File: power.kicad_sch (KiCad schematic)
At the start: 43 parts, among them SW2 SW_DPST

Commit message: more traces
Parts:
- added C49: 220uF, Capacitor_THT:CP_Radial_Tantal_D8.0mm_P5.00mm, symbol Device:C_Polarized_Small
- added C70: 33nF, Capacitor_SMD:C_0805_2012Metric, symbol Device:C_Small
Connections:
- net +5C: now also C70.2
- net +5V: now also C49.1
- net GND: now also C49.2, C70.1
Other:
- moved on the sheet: C24, C37, C38, C40, C50, C64, C66, C67

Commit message: keyboard routing
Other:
- moved on the sheet: C103, C138, C151, C227, C71, C85, C91, C92, C95

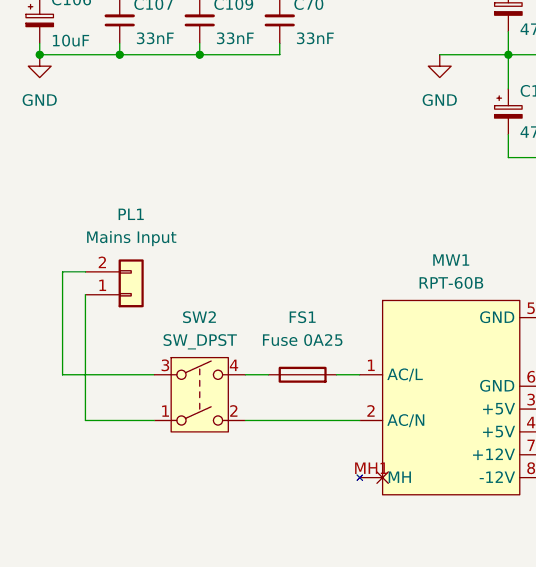
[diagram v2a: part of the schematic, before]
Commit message: progress power and keyboard
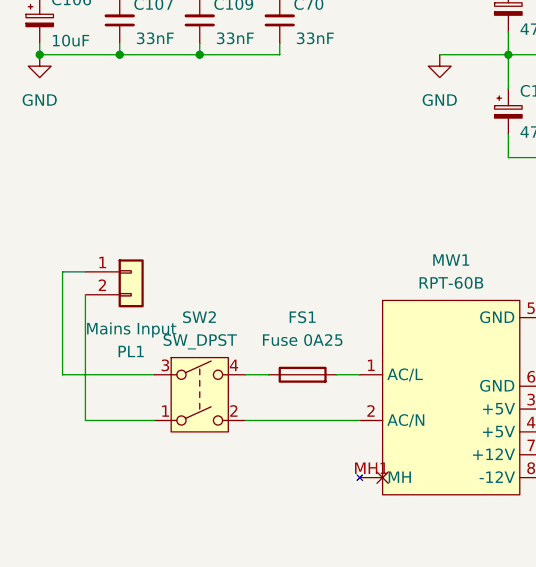
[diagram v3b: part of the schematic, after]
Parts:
- PL1: footprint Connector_Molex:Molex_KK-396_A-41792-0002_1x02_P3.96mm_Horizontal -> Acorn:AC_Power_Header
- SW2: footprint Button_Switch_THT:SW_Push_2P1T_Toggle_CK_PVA1xxH1xxxxxxV2 -> Acorn:Power_Switch
- TP2, TP3: footprint Acorn:Molex_19708-4003 -> Connector_PinHeader_2.54mm:PinHeader_1x01_P2.54mm_Vertical
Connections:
- net at PL1.1 (Pin_1): now also SW2.3; no longer SW2.1
- net at PL1.2 (Pin_2): now also SW2.1; no longer SW2.3
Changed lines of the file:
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@@
 	(wire
 		(pts
-			(xy 35.56 71.12) (xy 35.56 85.09)
-		)
-		(stroke
-			(width 0)
-			(type default)
-		)
-	)
-	(wire
-		(pts
 			(xy 231.14 27.94) (xy 231.14 29.21)
 		)
@@
 	(wire
 		(pts
+			(xy 35.56 71.12) (xy 35.56 85.09)
+		)
+		(stroke
+			(width 0)
+			(type default)
+		)
+	)
+	(wire
+		(pts
 			(xy 231.14 29.21) (xy 222.25 29.21)
 		)
@@
 	(symbol
 		(lib_id "Connector_Generic:Conn_01x02")
-		(at 40.64 71.12 0)
-		(mirror x)
+		(at 40.64 68.58 0)
 		(unit 1)
 		(exclude_from_sim no)
@@
 		(on_board yes)
 		(dnp no)
-		(fields_autoplaced yes)
 		(property "Reference" "PL1"
-			(at 40.64 62.23 0)
+			(at 40.64 77.47 0)
 			(effects
 				(font
@@
 		)
 		(property "Value" "Mains Input"
-			(at 40.64 64.77 0)
+			(at 40.64 74.93 0)
 			(effects
 				(font
@@
 			)
 		)
-		(property "Footprint" "Connector_Molex:Molex_KK-396_A-41792-0002_1x02_P3.96mm_Horizontal"
-			(at 40.64 71.12 0)
+		(property "Footprint" "Acorn:AC_Power_Header"
+			(at 40.64 68.58 0)
 			(effects
 				(font
@@
 		)
 		(property "Datasheet" "~"
-			(at 40.64 71.12 0)
+			(at 40.64 68.58 0)
 			(effects
 				(font
@@
 		)
 		(property "Description" "Generic connector, single row, 01x02, script generated (kicad-library-utils/schlib/autogen/connector/)"
-			(at 40.64 71.12 0)
+			(at 40.64 68.58 0)
 			(effects
 				(font
@@
 		(exclude_from_sim no)
 		(in_bom yes)
-		(on_board no)
+		(on_board yes)
 		(dnp no)
 		(fields_autoplaced yes)
@@
 			)
 		)
-		(property "Footprint" "Button_Switch_THT:SW_Push_2P1T_Toggle_CK_PVA1xxH1xxxxxxV2"
+		(property "Footprint" "Acorn:Power_Switch"
 			(at 48.26 82.55 0)
 			(effects
@@
 			)
 		)
-		(property "Footprint" "Acorn:Molex_19708-4003"
+		(property "Footprint" "Connector_PinHeader_2.54mm:PinHeader_1x01_P2.54mm_Vertical"
 			(at 118.11 69.85 0)
 			(effects
@@
 			)
 		)
-		(property "Footprint" "Acorn:Molex_19708-4003"
+		(property "Footprint" "Connector_PinHeader_2.54mm:PinHeader_1x01_P2.54mm_Vertical"
 			(at 109.22 69.85 0)
 			(effects

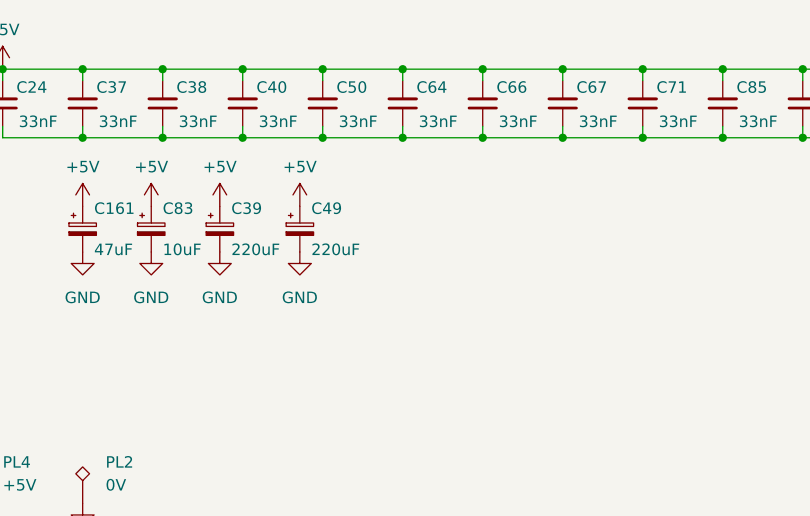
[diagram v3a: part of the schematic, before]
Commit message: add missing capacitors
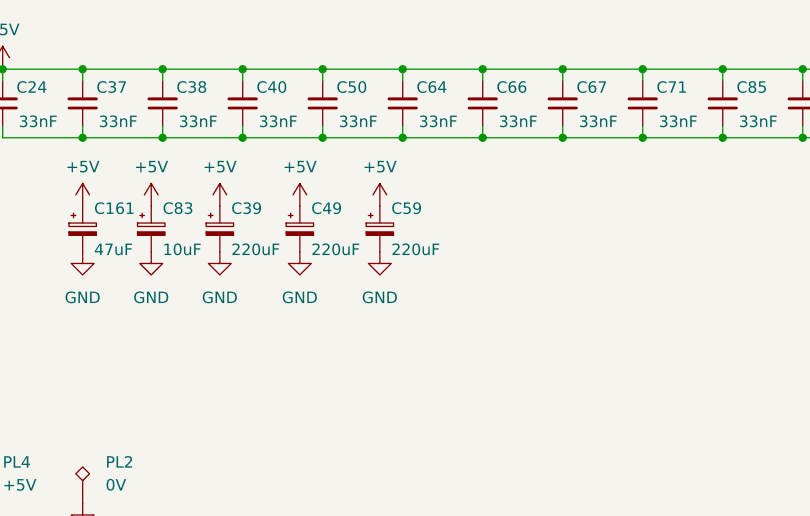
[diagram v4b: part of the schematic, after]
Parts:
- added C59: 220uF, Capacitor_THT:CP_Radial_Tantal_D8.0mm_P5.00mm, symbol Device:C_Polarized_Small
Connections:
- net +5V: now also C59.1
- net GND: now also C59.2
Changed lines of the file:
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@@
 	)
 	(symbol
+		(lib_id "power:GND")
+		(at 166.37 41.91 0)
+		(unit 1)
+		(exclude_from_sim no)
+		(in_bom yes)
+		(on_board yes)
+		(dnp no)
+		(fields_autoplaced yes)
+		(property "Reference" "#PWR0307"
+			(at 166.37 48.26 0)
+			(effects
+				(font
+					(size 1.27 1.27)
+				)
+				(hide yes)
+			)
+		)
+		(property "Value" "GND"
+			(at 166.37 46.99 0)
+			(effects
+				(font
+					(size 1.27 1.27)
+				)
+			)
+		)
+		(property "Footprint" ""
+			(at 166.37 41.91 0)
+			(effects
+				(font
+					(size 1.27 1.27)
+				)
+				(hide yes)
+			)
+		)
+		(property "Datasheet" ""
+			(at 166.37 41.91 0)
+			(effects
+				(font
+					(size 1.27 1.27)
+				)
+				(hide yes)
+			)
+		)
+		(property "Description" "Power symbol creates a global label with name \"GND\" , ground"
+			(at 166.37 41.91 0)
+			(effects
+				(font
+					(size 1.27 1.27)
+				)
+				(hide yes)
+			)
+		)
+		(pin "1"
+		)
+		(instances
+			(project "Acorn-A3010"
+				(path "/999882f3-94f8-4a89-9093-27a47d0cb289/5e8722fb-7afe-44d4-8a36-2936df1b76c5"
+					(reference "#PWR0307")
+					(unit 1)
+				)
+			)
+		)
+	)
+	(symbol
 		(lib_id "power:+5V")
 		(at 140.97 36.83 0)
@@
 	)
 	(symbol
+		(lib_id "Device:C_Polarized_Small")
+		(at 166.37 39.37 0)
+		(unit 1)
+		(exclude_from_sim no)
+		(in_bom yes)
+		(on_board yes)
+		(dnp no)
+		(property "Reference" "C59"
+			(at 167.64 37.084 0)
+			(effects
+				(font
+					(size 1.27 1.27)
+				)
+				(justify left)
+			)
+		)
+		(property "Value" "220uF"
+			(at 167.64 41.656 0)
+			(effects
+				(font
+					(size 1.27 1.27)
+				)
+				(justify left)
+			)
+		)
+		(property "Footprint" "Capacitor_THT:CP_Radial_Tantal_D8.0mm_P5.00mm"
+			(at 166.37 39.37 0)
+			(effects
+				(font
+					(size 1.27 1.27)
+				)
+				(hide yes)
+			)
+		)
+		(property "Datasheet" "~"
+			(at 166.37 39.37 0)
+			(effects
+				(font
+					(size 1.27 1.27)
+				)
+				(hide yes)
+			)
+		)
+		(property "Description" "Polarized capacitor, small symbol"
+			(at 166.37 39.37 0)
+			(effects
+				(font
+					(size 1.27 1.27)
+				)
+				(hide yes)
+			)
+		)
+		(pin "2"
+		)
+		(pin "1"
+		)
+		(instances
+			(project "Acorn-A3010"
+				(path "/999882f3-94f8-4a89-9093-27a47d0cb289/5e8722fb-7afe-44d4-8a36-2936df1b76c5"
+					(reference "C59")
+					(unit 1)
+				)
+			)
+		)
+	)
+	(symbol
 		(lib_id "Device:Fuse")
 		(at 59.69 80.01 90)
@@
 					(unit 1)
 				)
+			)
+		)
+	)
+	(symbol
+		(lib_id "power:+5V")
+		(at 166.37 36.83 0)
+		(unit 1)
+		(exclude_from_sim no)
+		(in_bom yes)
+		(on_board yes)
+		(dnp no)
+		(fields_autoplaced yes)
+		(property "Reference" "#PWR0267"
+			(at 166.37 40.64 0)
+			(effects
+				(font
+					(size 1.27 1.27)
+				)
+				(hide yes)
+			)
+		)
+		(property "Value" "+5V"
+			(at 166.37 32.4587 0)
+			(effects
+				(font
+					(size 1.27 1.27)
+				)
+			)
+		)
+		(property "Footprint" ""
+			(at 166.37 36.83 0)
+			(effects
+				(font
+					(size 1.27 1.27)
+				)
+				(hide yes)
+			)
+		)
+		(property "Datasheet" ""
+			(at 166.37 36.83 0)
+			(effects
+				(font
+					(size 1.27 1.27)
+				)
+				(hide yes)
+			)
+		)
+		(property "Description" "Power symbol creates a global label with name \"+5V\""
+			(at 166.37 36.83 0)
+			(effects
+				(font
+					(size 1.27 1.27)
+				)
+				(hide yes)
+			)
+		)
+		(pin "1"
+		)
+		(instances
+			(project "Acorn-A3010"
+				(path "/999882f3-94f8-4a89-9093-27a47d0cb289/5e8722fb-7afe-44d4-8a36-2936df1b76c5"
+					(reference "#PWR0267")
+					(unit 1)
+				)

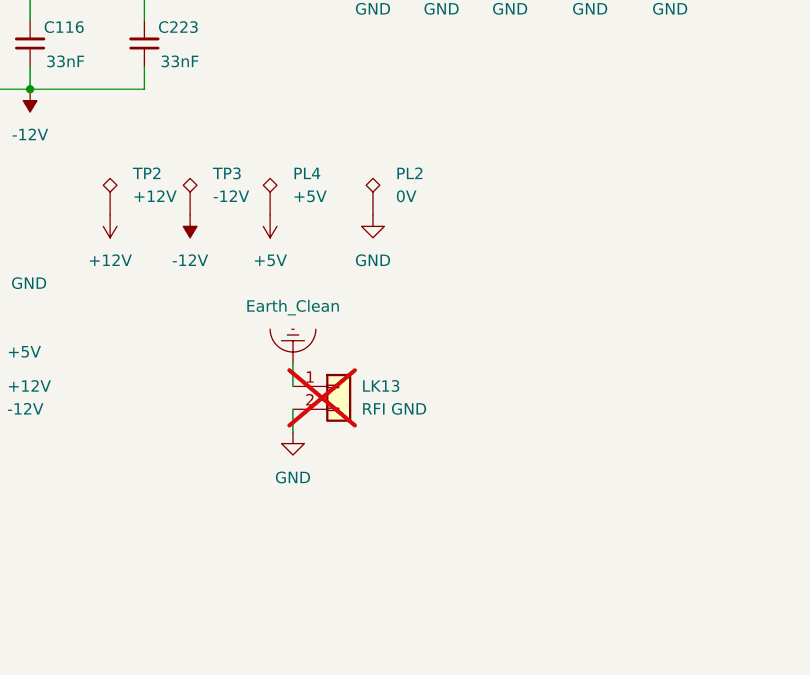
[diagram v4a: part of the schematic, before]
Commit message: adjust shielding perimeter trace and mounting holes
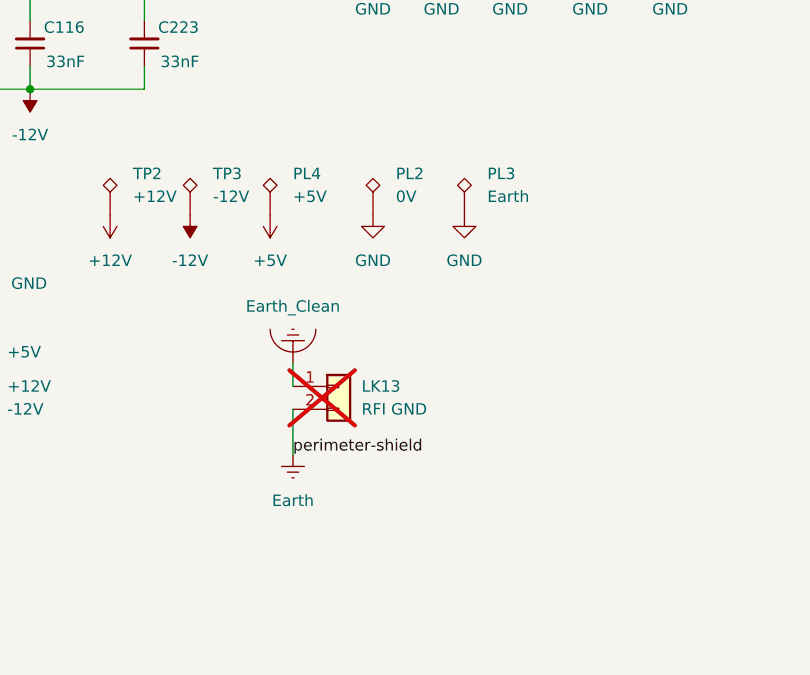
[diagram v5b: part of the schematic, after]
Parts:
- added PL3: Earth, Acorn:Molex_19708-4003, symbol Connector:TestPoint_Alt
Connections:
- net GND: now also PL3.1; no longer LK13.2 (Pin_2)
- new net Earth: LK13.2 (Pin_2)
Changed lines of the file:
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@@
 	(wire
 		(pts
-			(xy 124.46 91.44) (xy 124.46 93.98)
+			(xy 124.46 91.44) (xy 124.46 96.52)
 		)
 		(stroke
@@
 		)
 	)
+	(label "perimeter-shield"
+		(at 124.46 96.52 0)
+		(effects
+			(font
+				(size 1.27 1.27)
+			)
+			(justify left bottom)
+		)
+	)
 	(symbol
 		(lib_id "Device:C_Small")
@@
 	)
 	(symbol
+		(lib_id "power:Earth")
+		(at 124.46 96.52 0)
+		(unit 1)
+		(exclude_from_sim no)
+		(in_bom yes)
+		(on_board yes)
+		(dnp no)
+		(fields_autoplaced yes)
+		(property "Reference" "#PWR0310"
+			(at 124.46 102.87 0)
+			(effects
+				(font
+					(size 1.27 1.27)
+				)
+				(hide yes)
+			)
+		)
+		(property "Value" "Earth"
+			(at 124.46 101.6 0)
+			(effects
+				(font
+					(size 1.27 1.27)
+				)
+			)
+		)
+		(property "Footprint" ""
+			(at 124.46 96.52 0)
+			(effects
+				(font
+					(size 1.27 1.27)
+				)
+				(hide yes)
+			)
+		)
+		(property "Datasheet" "~"
+			(at 124.46 96.52 0)
+			(effects
+				(font
+					(size 1.27 1.27)
+				)
+				(hide yes)
+			)
+		)
+		(property "Description" "Power symbol creates a global label with name \"Earth\""
+			(at 124.46 96.52 0)
+			(effects
+				(font
+					(size 1.27 1.27)
+				)
+				(hide yes)
+			)
+		)
+		(pin "1"
+		)
+		(instances
+			(project ""
+				(path "/999882f3-94f8-4a89-9093-27a47d0cb289/5e8722fb-7afe-44d4-8a36-2936df1b76c5"
+					(reference "#PWR0310")
+					(unit 1)
+				)
+			)
+		)
+	)
+	(symbol
 		(lib_id "Device:C_Small")
 		(at 95.25 50.8 180)
@@
 	)
 	(symbol
+		(lib_id "Connector:TestPoint_Alt")
+		(at 143.51 69.85 0)
+		(unit 1)
+		(exclude_from_sim no)
+		(in_bom yes)
+		(on_board yes)
+		(dnp no)
+		(fields_autoplaced yes)
+		(property "Reference" "PL3"
+			(at 146.05 65.2779 0)
+			(effects
+				(font
+					(size 1.27 1.27)
+				)
+				(justify left)
+			)
+		)
+		(property "Value" "Earth"
+			(at 146.05 67.8179 0)
+			(effects
+				(font
+					(size 1.27 1.27)
+				)
+				(justify left)
+			)
+		)
+		(property "Footprint" "Acorn:Molex_19708-4003"
+			(at 148.59 69.85 0)
+			(effects
+				(font
+					(size 1.27 1.27)
+				)
+				(hide yes)
+			)
+		)
+		(property "Datasheet" "~"
+			(at 148.59 69.85 0)
+			(effects
+				(font
+					(size 1.27 1.27)
+				)
+				(hide yes)
+			)
+		)
+		(property "Description" "test point (alternative shape)"
+			(at 143.51 69.85 0)
+			(effects
+				(font
+					(size 1.27 1.27)
+				)
+				(hide yes)
+			)
+		)
+		(pin "1"
+		)
+		(instances
+			(project "Acorn-A3010"
+				(path "/999882f3-94f8-4a89-9093-27a47d0cb289/5e8722fb-7afe-44d4-8a36-2936df1b76c5"
+					(reference "PL3")
+					(unit 1)
+				)
+			)
+		)
+	)
+	(symbol
 		(lib_id "Device:C_Small")
 		(at 204.47 25.4 180)
@@
 	)
 	(symbol
+		(lib_id "power:GND")
+		(at 143.51 69.85 0)
+		(unit 1)
+		(exclude_from_sim no)
+		(in_bom yes)
+		(on_board yes)
+		(dnp no)
+		(fields_autoplaced yes)
+		(property "Reference" "#PWR0197"
+			(at 143.51 76.2 0)
+			(effects
+				(font
+					(size 1.27 1.27)
+				)
+				(hide yes)
+			)
+		)
+		(property "Value" "GND"
+			(at 143.51 74.93 0)
+			(effects
+				(font
+					(size 1.27 1.27)
+				)
+			)
+		)
+		(property "Footprint" ""
+			(at 143.51 69.85 0)
+			(effects
+				(font
+					(size 1.27 1.27)
+				)
+				(hide yes)
+			)
+		)
+		(property "Datasheet" ""
+			(at 143.51 69.85 0)
+			(effects
+				(font
+					(size 1.27 1.27)
+				)
+				(hide yes)
+			)
+		)
+		(property "Description" "Power symbol creates a global label with name \"GND\" , ground"
+			(at 143.51 69.85 0)
+			(effects
+				(font
+					(size 1.27 1.27)
+				)
+				(hide yes)
+			)
+		)
+		(pin "1"
+		)
+		(instances
+			(project "Acorn-A3010"
+				(path "/999882f3-94f8-4a89-9093-27a47d0cb289/5e8722fb-7afe-44d4-8a36-2936df1b76c5"
+					(reference "#PWR0197")
+					(unit 1)
+				)
+			)
+		)
+	)
+	(symbol
 		(lib_id "Switch:SW_DPST")
 		(at 48.26 82.55 0)
@@
 					(unit 1)
 				)
-			)
-		)
-	)
-	(symbol
-		(lib_id "power:GND")
-		(at 124.46 93.98 0)
-		(unit 1)
-		(exclude_from_sim no)
-		(in_bom yes)
-		(on_board yes)
-		(dnp no)
-		(fields_autoplaced yes)
-		(property "Reference" "#PWR0197"
-			(at 124.46 100.33 0)
-			(effects
-				(font
-					(size 1.27 1.27)
-				)
-				(hide yes)
-			)
-		)
-		(property "Value" "GND"
-			(at 124.46 99.06 0)
-			(effects
-				(font
-					(size 1.27 1.27)
-				)
-			)
-		)
-		(property "Footprint" ""
-			(at 124.46 93.98 0)
-			(effects
-				(font
-					(size 1.27 1.27)
-				)
-				(hide yes)
-			)
-		)
-		(property "Datasheet" ""
-			(at 124.46 93.98 0)
-			(effects
-				(font
-					(size 1.27 1.27)
-				)
-				(hide yes)
-			)
-		)
-		(property "Description" "Power symbol creates a global label with name \"GND\" , ground"
-			(at 124.46 93.98 0)
-			(effects
-				(font
-					(size 1.27 1.27)
-				)
-				(hide yes)
-			)
-		)
-		(pin "1"
-		)
-		(instances
-			(project "Acorn-A3010"
-				(path "/999882f3-94f8-4a89-9093-27a47d0cb289/5e8722fb-7afe-44d4-8a36-2936df1b76c5"
-					(reference "#PWR0197")
-					(unit 1)
-				)

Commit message: add ide and rework onboard ram
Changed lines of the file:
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@@
 (kicad_sch
-	(version 20231120)
+	(version 20250114)
 	(generator "eeschema")
-	(generator_version "8.0")
+	(generator_version "9.0")
 	(paper "A4")
 	(junction
@@
 		)
 		(instances
-			(project ""
+			(project "Acorn-A3010"
 				(path "/999882f3-94f8-4a89-9093-27a47d0cb289/5e8722fb-7afe-44d4-8a36-2936df1b76c5"
 					(reference "#PWR0184")
@@
 		)
 		(instances
-			(project ""
+			(project "Acorn-A3010"
 				(path "/999882f3-94f8-4a89-9093-27a47d0cb289/5e8722fb-7afe-44d4-8a36-2936df1b76c5"
 					(reference "FS1")
@@
 		)
 		(instances
-			(project ""
+			(project "Acorn-A3010"
 				(path "/999882f3-94f8-4a89-9093-27a47d0cb289/5e8722fb-7afe-44d4-8a36-2936df1b76c5"
 					(reference "MW1")
@@
 		)
 		(instances
-			(project ""
+			(project "Acorn-A3010"
 				(path "/999882f3-94f8-4a89-9093-27a47d0cb289/5e8722fb-7afe-44d4-8a36-2936df1b76c5"
 					(reference "PL1")
@@
 		)
 		(instances
-			(project ""
+			(project "Acorn-A3010"
 				(path "/999882f3-94f8-4a89-9093-27a47d0cb289/5e8722fb-7afe-44d4-8a36-2936df1b76c5"
 					(reference "PL5")
@@
 		)
 		(instances
-			(project ""
+			(project "Acorn-A3010"
 				(path "/999882f3-94f8-4a89-9093-27a47d0cb289/5e8722fb-7afe-44d4-8a36-2936df1b76c5"
 					(reference "#PWR0310")
@@
 		)
 		(instances
-			(project ""
+			(project "Acorn-A3010"
 				(path "/999882f3-94f8-4a89-9093-27a47d0cb289/5e8722fb-7afe-44d4-8a36-2936df1b76c5"
 					(reference "#PWR0198")
@@
 		)
 		(instances
-			(project ""
+			(project "Acorn-A3010"
 				(path "/999882f3-94f8-4a89-9093-27a47d0cb289/5e8722fb-7afe-44d4-8a36-2936df1b76c5"
 					(reference "SW2")
@@
 		)
 		(instances
-			(project ""
+			(project "Acorn-A3010"
 				(path "/999882f3-94f8-4a89-9093-27a47d0cb289/5e8722fb-7afe-44d4-8a36-2936df1b76c5"
 					(reference "LK13")
@@
 		)
 		(instances
-			(project ""
+			(project "Acorn-A3010"
 				(path "/999882f3-94f8-4a89-9093-27a47d0cb289/5e8722fb-7afe-44d4-8a36-2936df1b76c5"
 					(reference "PL4")
@@
 		)
 		(instances
-			(project ""
+			(project "Acorn-A3010"
 				(path "/999882f3-94f8-4a89-9093-27a47d0cb289/5e8722fb-7afe-44d4-8a36-2936df1b76c5"
 					(reference "#PWR0188")
@@
 		)
 		(instances
-			(project ""
+			(project "Acorn-A3010"
 				(path "/999882f3-94f8-4a89-9093-27a47d0cb289/5e8722fb-7afe-44d4-8a36-2936df1b76c5"
 					(reference "#PWR0187")
@@
 		)
 		(instances
-			(project ""
+			(project "Acorn-A3010"
 				(path "/999882f3-94f8-4a89-9093-27a47d0cb289/5e8722fb-7afe-44d4-8a36-2936df1b76c5"
 					(reference "#PWR0183")
